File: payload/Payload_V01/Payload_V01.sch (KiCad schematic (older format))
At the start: 0 parts

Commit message: added schematic for rf generator
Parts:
- added 0.1uF: C, symbol Device:C
- added C? (x2): 1uF, symbol Device:C
- added C? (x11): 0.1uF, symbol Device:C
- added C?: 0.01uF, symbol Device:C
- added C?: 10uF, symbol Device:C
- added C? (x2): 10uF, symbol Device:CP
- added J? (x3): Conn_Coaxial, symbol Connector:Conn_Coaxial
- added J? (x2): Screw_Terminal_01x02, symbol Connector:Screw_Terminal_01x02
- added JP?: Jumper, symbol Device:Jumper
- added JP? (x3): Jumper_3_Open, symbol Jumper:Jumper_3_Open
- added R?: 6.8k, symbol Device:R_US
- added R? (x2): 200, symbol Device:R_US
- added R?: 300, symbol Device:R_US
- added R? (x5): 0, symbol Device:R_US
- added U?: AD9838, symbol Payload_V01:AD9838
- added U?: REF196, symbol Reference_Voltage:REF196
- added Y?: SG-310SCF, symbol Payload_V01:SG-310SCF
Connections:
- new net: C?.2, C?.2, JP?.2 (C), U?.1 (AVDD)
- new net: J?.1 (In), U?.13 (SIGN_BIT_OUT)
- new net: 0.1uF.1, R?.2, U?.14 (VIN)
- new net: C?.1, J?.1 (In), R?.1, R?.2, U?.16 (IOUT)
- new net: C?.1, J?.1 (In), R?.1, U?.17 (IOUTB)
- new net: C?.2, R?.2, U?.18 (FSADJUST)
- new net: C?.2, U?.19 (REFOUT)
- new net: C?.1, U?.20 (COMP)
- new net: C?.1, C?.1, JP?.1, U?.3 (CAP/2.5V)
- new net: R?.1, U?.5 (MCLK)
- new net: R?.1, U?.6 (FSELECT)
- new net: R?.1, U?.7 (PSELECT)
- new net: R?.1, U?.8 (RESET)
- new net: R?.1, U?.9 (SLEEP)
- new net: R?.2, Y?.3 (O/P)
- new net: JP?.2 (C), Y?.4 (VDD)
- new net: C?.1, C?.1, JP?.1 (A), U?.6 (Vout)
- new net 3.3V_BF: JP?.3 (B), JP?.3 (B)
- new net 5V_EXT: C?.1, C?.1, U?.2 (Vin), U?.3 (~Sleep~)
- new net DVDD_1: C?.1, JP?.2, JP?.2 (C), U?.2 (DVDD)
- new net FSEL: R?.2
- new net FSYNC: U?.12 (FSYNC)
- new net GND: 0.1uF.2, C?.1, C?.1, C?.1, C?.2, C?.2, C?.2, C?.2, C?.2, C?.2, C?.2, C?.2, C?.2, C?.2, C?.2, C?.2, C?.2, J?.2 (Ext), J?.2 (Ext), J?.2 (Ext), J?.2 (Pin_2), J?.2 (Pin_2), R?.1, R?.1, R?.2, U?.15 (AGND), U?.4 (DGND), U?.4 (GND), Y?.2 (GND)
- new net PSEL: R?.2
- new net RESET: R?.2
- new net SCLK: U?.11 (SCLK)
- new net SDATA: U?.10 (SDATA)
- new net SLEEP: R?.2
- new net VDD: C?.1, C?.1, J?.1 (Pin_1), JP?.1 (A), JP?.3 (B)
- new net VDDA: C?.1, C?.1, J?.1 (Pin_1), JP?.1 (A)

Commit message: updates to schematic
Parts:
- C1, C10, C11, C12, C13, C14, C15, C17, C2, C3, C4, C7, C8, C9: renamed from C?; footprint (none) -> Capacitor_SMD:C_0603_1608Metric_Pad1.05x0.95mm_HandSolder
- C16: renamed from 0.1uF; value C -> 0.1uF; footprint (none) -> Capacitor_SMD:C_0603_1608Metric_Pad1.05x0.95mm_HandSolder
- C18: renamed from C?; footprint (none) -> Capacitor_SMD:C_0805_2012Metric_Pad1.15x1.40mm_HandSolder
- C5, C6: renamed from C?; footprint (none) -> Capacitor_Tantalum_SMD:CP_EIA-3216-18_Kemet-A_Pad1.58x1.35mm_HandSolder
- J1, J2: renamed from J?; footprint (none) -> TerminalBlock:TerminalBlock_Altech_AK300-2_P5.00mm
- J3, J4, J5: renamed from J?; footprint (none) -> Connector_Coaxial:SMB_Jack_Vertical
- R1, R2, R3, R4, R5, R6, R7, R8, R9: renamed from R?; footprint (none) -> Resistor_SMD:R_0603_1608Metric_Pad1.05x0.95mm_HandSolder
- gave numbers to parts that had none: 7

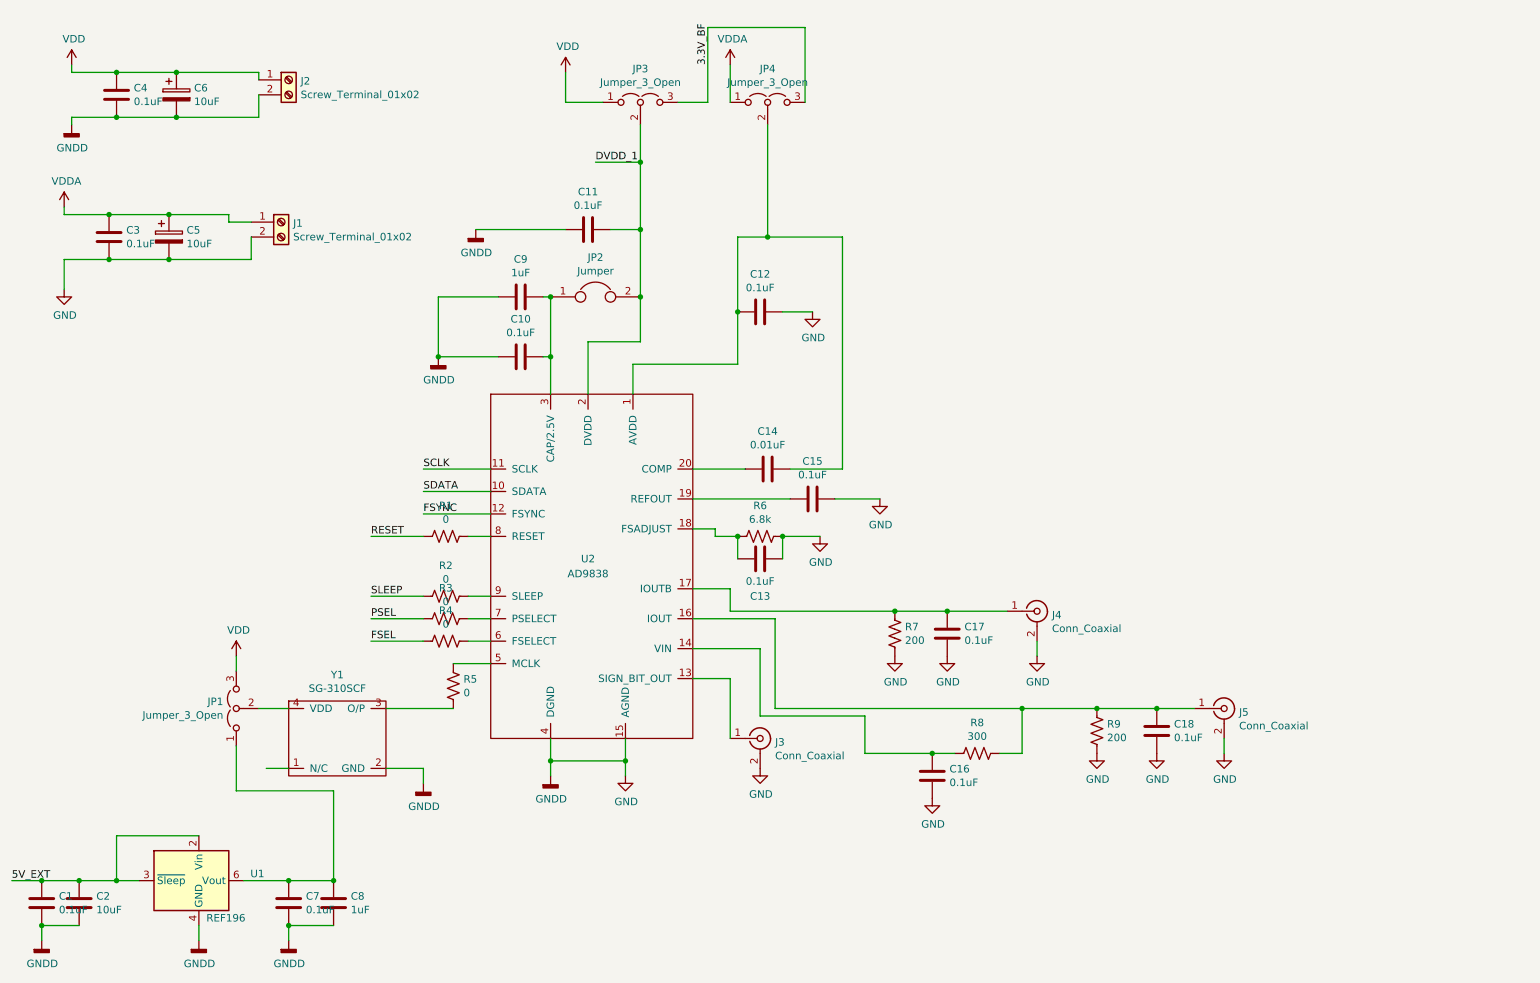
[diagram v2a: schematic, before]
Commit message: created new schematic sheets for each part
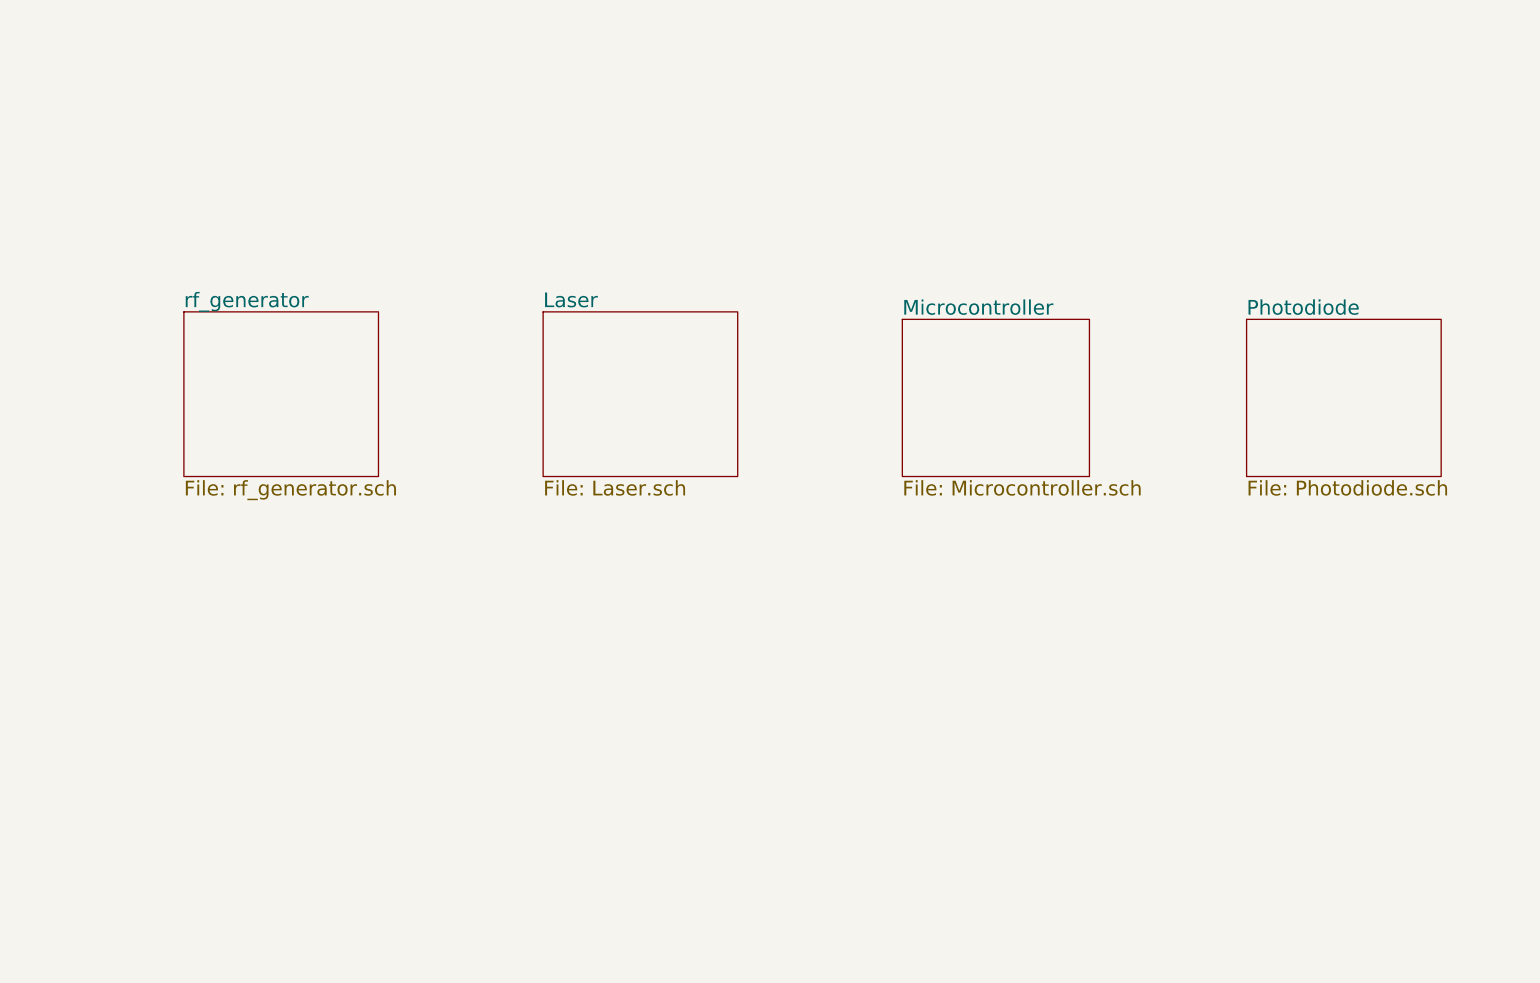
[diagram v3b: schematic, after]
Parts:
- removed C1, C10, C11, C12, C13, C15, C16, C17, C3, C4, C7: 0.1uF, Capacitor_SMD:C_0603_1608Metric_Pad1.05x0.95mm_HandSolder, symbol Device:C
- removed C14: 0.01uF, Capacitor_SMD:C_0603_1608Metric_Pad1.05x0.95mm_HandSolder, symbol Device:C
- removed C18: 0.1uF, Capacitor_SMD:C_0805_2012Metric_Pad1.15x1.40mm_HandSolder, symbol Device:C
- removed C2: 10uF, Capacitor_SMD:C_0603_1608Metric_Pad1.05x0.95mm_HandSolder, symbol Device:C
- removed C5, C6: 10uF, Capacitor_Tantalum_SMD:CP_EIA-3216-18_Kemet-A_Pad1.58x1.35mm_HandSolder, symbol Device:CP
- removed C8, C9: 1uF, Capacitor_SMD:C_0603_1608Metric_Pad1.05x0.95mm_HandSolder, symbol Device:C
- removed J1, J2: Screw_Terminal_01x02, TerminalBlock:TerminalBlock_Altech_AK300-2_P5.00mm, symbol Connector:Screw_Terminal_01x02
- removed J3, J4, J5: Conn_Coaxial, Connector_Coaxial:SMB_Jack_Vertical, symbol Connector:Conn_Coaxial
- removed JP1, JP3, JP4: Jumper_3_Open, symbol Jumper:Jumper_3_Open
- removed JP2: Jumper, symbol Device:Jumper
- removed R1, R2, R3, R4, R5: 0, Resistor_SMD:R_0603_1608Metric_Pad1.05x0.95mm_HandSolder, symbol Device:R_US
- removed R6: 6.8k, Resistor_SMD:R_0603_1608Metric_Pad1.05x0.95mm_HandSolder, symbol Device:R_US
- removed R7, R9: 200, Resistor_SMD:R_0603_1608Metric_Pad1.05x0.95mm_HandSolder, symbol Device:R_US
- removed R8: 300, Resistor_SMD:R_0603_1608Metric_Pad1.05x0.95mm_HandSolder, symbol Device:R_US
- removed U1: REF196, symbol Reference_Voltage:REF196
- removed U2: AD9838, symbol Payload_V01:AD9838
- removed Y1: SG-310SCF, symbol Payload_V01:SG-310SCF

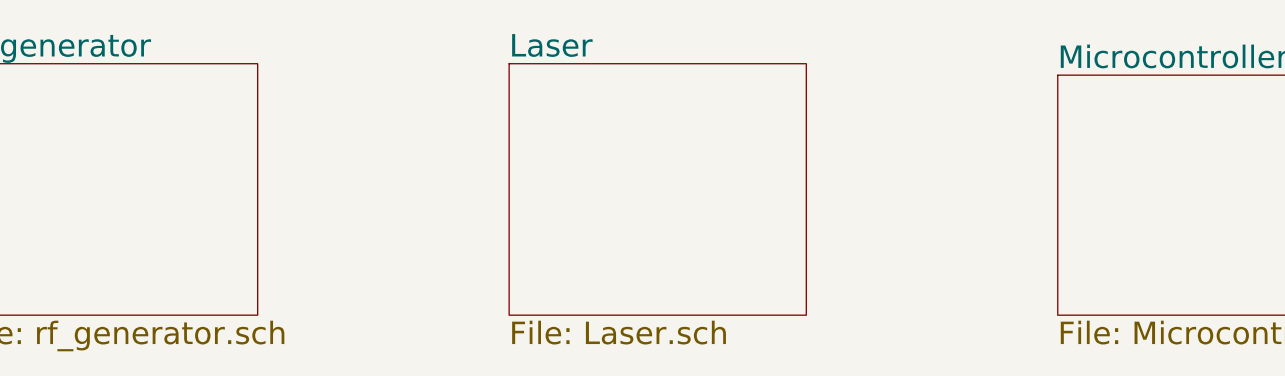
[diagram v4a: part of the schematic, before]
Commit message: tested labels to get microcontroller working
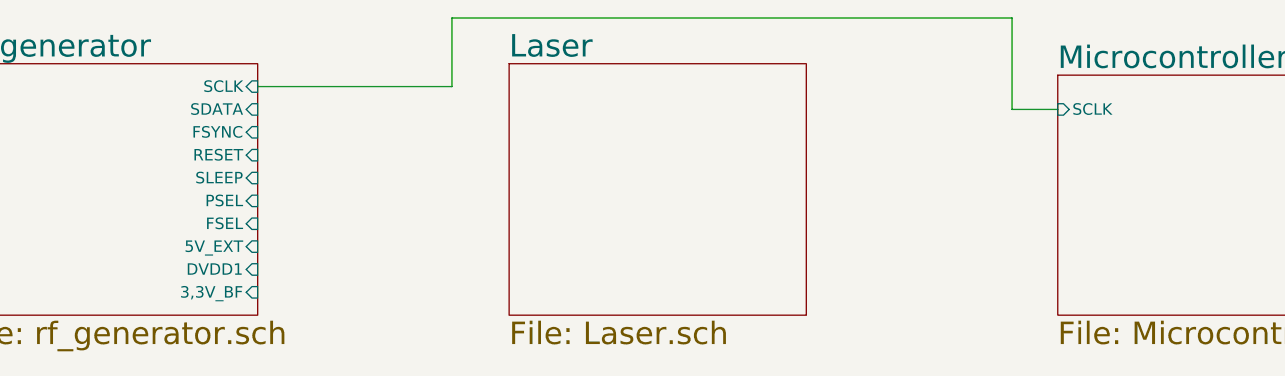
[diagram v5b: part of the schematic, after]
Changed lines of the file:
@@
 F0 "rf_generator" 98
 F1 "rf_generator.sch" 98
+F2 "SCLK" I R 3100 2700 50
+F3 "SDATA" I R 3100 2800 50
+F4 "FSYNC" I R 3100 2900 50
+F5 "RESET" I R 3100 3000 50
+F6 "SLEEP" I R 3100 3100 50
+F7 "PSEL" I R 3100 3200 50
+F8 "FSEL" I R 3100 3300 50
+F9 "5V_EXT" I R 3100 3400 50
+F10 "DVDD1" I R 3100 3500 50
+F11 "3,3V_BF" I R 3100 3600 50
 $EndSheet
 $Sheet
@@
 F0 "Microcontroller" 98
 F1 "Microcontroller.sch" 98
+F2 "SCLK" I L 6600 2800 50
 $EndSheet
 $Sheet
@@
 F1 "Photodiode.sch" 98
 $EndSheet
+Wire Wire Line
+	3100 2700 3950 2700
+Wire Wire Line
+	3950 2700 3950 2400
+Wire Wire Line
+	3950 2400 6400 2400
+Wire Wire Line
+	6400 2400 6400 2800
+Wire Wire Line
+	6400 2800 6600 2800
 $EndSCHEMATC

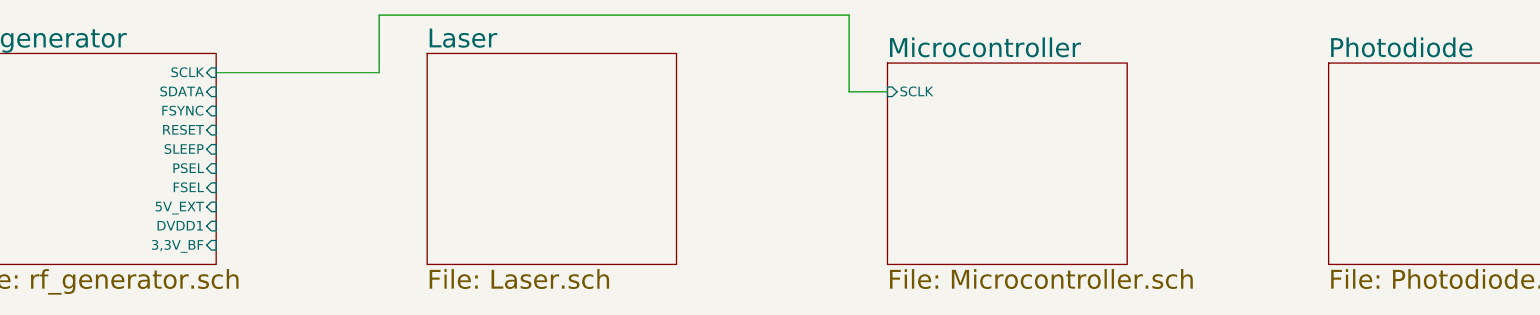
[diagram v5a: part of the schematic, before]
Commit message: added some more pins
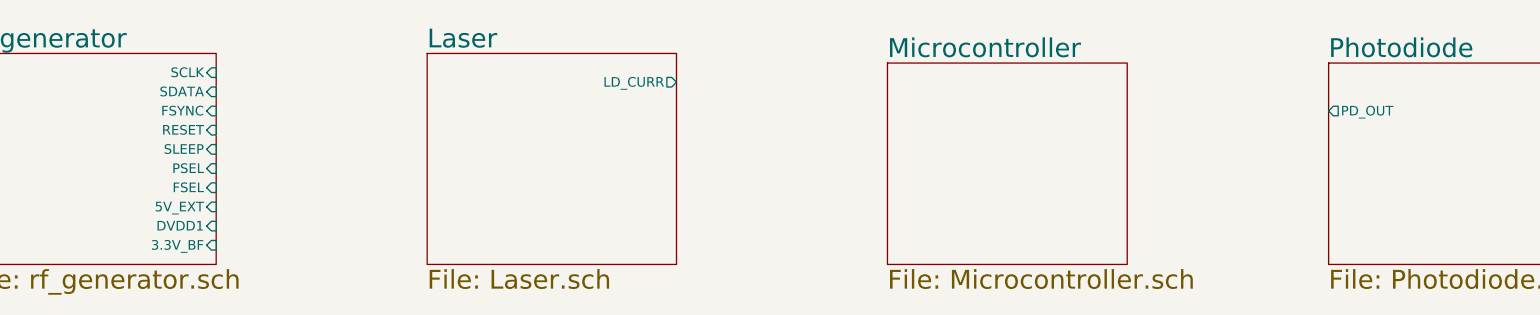
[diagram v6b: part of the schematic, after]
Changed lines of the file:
@@
 F9 "5V_EXT" I R 3100 3400 50
 F10 "DVDD1" I R 3100 3500 50
-F11 "3,3V_BF" I R 3100 3600 50
+F11 "3.3V_BF" I R 3100 3600 50
 $EndSheet
 $Sheet
@@
 F0 "Laser" 98
 F1 "Laser.sch" 98
+F2 "LD_CURR" O R 5500 2750 50
 $EndSheet
 $Sheet
@@
 F0 "Microcontroller" 98
 F1 "Microcontroller.sch" 98
-F2 "SCLK" I L 6600 2800 50
 $EndSheet
 $Sheet
@@
 F0 "Photodiode" 98
 F1 "Photodiode.sch" 98
+F2 "PD_OUT" O L 8900 2900 50
 $EndSheet
-Wire Wire Line
-	3100 2700 3950 2700
-Wire Wire Line
-	3950 2700 3950 2400
-Wire Wire Line
-	3950 2400 6400 2400
-Wire Wire Line
-	6400 2400 6400 2800
-Wire Wire Line
-	6400 2800 6600 2800
 $EndSCHEMATC
